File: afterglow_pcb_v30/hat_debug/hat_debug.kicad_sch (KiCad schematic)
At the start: 95 parts, among them J1 Conn_01x04_Socket, J4 Conn_01x10_Pin, J5 Conn_01x10_Pin, J7 Conn_02x03_Odd_Even, J8 Conn_02x03_Odd_Even

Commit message: Removed wrong pin headers from production files
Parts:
- J7, J8: JLCPCB C92272 -> (none)
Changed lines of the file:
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@@
 			)
 		)
-		(property "JLCPCB" "C92272"
+		(property "JLCPCB" ""
 			(at 52.705 164.465 0)
 			(effects
@@
 			)
 		)
-		(property "JLCPCB" "C92272"
+		(property "JLCPCB" ""
 			(at 47.625 113.665 0)
 			(effects

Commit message: Fixed debug hat
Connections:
- net D_SCL: now also J8.3 (Pin_3); no longer J8.4 (Pin_4)
- net D_SDA: now also J8.6 (Pin_6); no longer J8.5 (Pin_5)
- net GND: now also J8.5 (Pin_5); no longer J8.6 (Pin_6)
- net OUT_CLK: now also J8.2 (Pin_2); no longer J8.1 (Pin_1)
- net OUT_DATA: now also J8.1 (Pin_1); no longer J8.2 (Pin_2)
- net OUT_LOAD: now also J8.4 (Pin_4); no longer J8.3 (Pin_3)
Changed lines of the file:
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@@
 	(symbol
 		(lib_id "Connector_Generic:Conn_02x03_Odd_Even")
-		(at 52.705 164.465 0)
+		(at 55.245 164.465 0)
+		(mirror y)
 		(unit 1)
 		(exclude_from_sim no)
@@
 		)
 		(property "Footprint" "Connector_PinHeader_2.54mm:PinHeader_2x03_P2.54mm_Vertical"
-			(at 52.705 164.465 0)
+			(at 55.245 164.465 0)
 			(effects
 				(font
@@
 		)
 		(property "Datasheet" "~"
-			(at 52.705 164.465 0)
+			(at 55.245 164.465 0)
 			(effects
 				(font
@@
 		)
 		(property "Description" ""
-			(at 52.705 164.465 0)
+			(at 55.245 164.465 0)
 			(effects
 				(font
@@
 		)
 		(property "JLCPCB" ""
-			(at 52.705 164.465 0)
+			(at 55.245 164.465 0)
 			(effects
 				(font

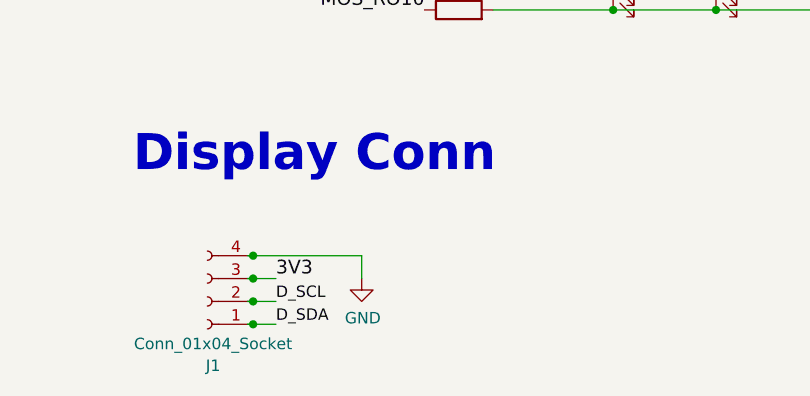
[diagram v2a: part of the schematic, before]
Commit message: Added i2c pullup resistors
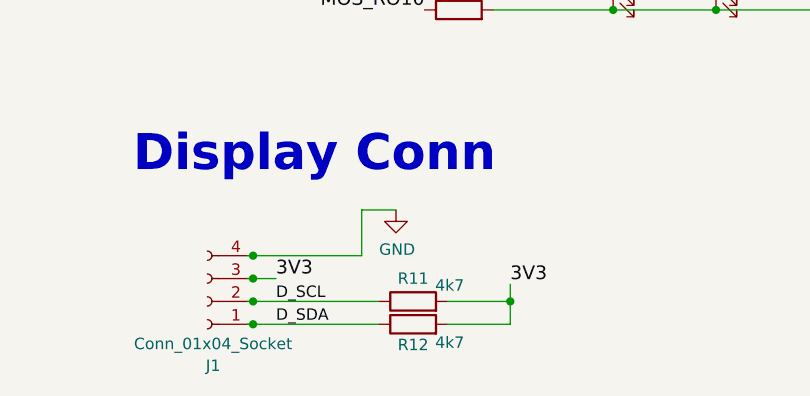
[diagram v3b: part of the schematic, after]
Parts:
- added R11, R12: 4k7, Resistor_SMD:R_0805_2012Metric, symbol Device:R
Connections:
- net 3V3: now also R11.2, R12.2
- net D_SCL: now also R11.1
- net D_SDA: now also R12.1
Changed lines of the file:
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@@
 	)
 	(junction
+		(at 149.225 177.8)
+		(diameter 0)
+		(color 0 0 0 0)
+	)
+	(junction
 		(at 206.375 122.555)
 		(diameter 0)
@@
 	(wire
 		(pts
+			(xy 149.225 175.895) (xy 149.225 177.8)
+		)
+		(stroke
+			(width 0)
+			(type default)
+		)
+	)
+	(wire
+		(pts
 			(xy 38.1 48.895) (xy 34.925 48.895)
 		)
@@
 	(wire
 		(pts
+			(xy 149.225 180.34) (xy 142.24 180.34)
+		)
+		(stroke
+			(width 0)
+			(type default)
+		)
+	)
+	(wire
+		(pts
 			(xy 194.945 88.265) (xy 183.515 88.265)
 		)
@@
 	(wire
 		(pts
+			(xy 149.225 177.8) (xy 149.225 180.34)
+		)
+		(stroke
+			(width 0)
+			(type default)
+		)
+	)
+	(wire
+		(pts
 			(xy 172.085 57.785) (xy 168.275 57.785)
 		)
@@
 	(wire
 		(pts
-			(xy 120.65 180.34) (xy 123.19 180.34)
+			(xy 120.65 180.34) (xy 134.62 180.34)
 		)
 		(stroke
@@
 	(wire
 		(pts
-			(xy 120.65 177.8) (xy 123.19 177.8)
+			(xy 120.65 177.8) (xy 134.62 177.8)
 		)
 		(stroke
@@
 	(wire
 		(pts
-			(xy 132.715 172.72) (xy 132.715 175.26)
-		)
-		(stroke
-			(width 0)
-			(type default)
-		)
-	)
-	(wire
-		(pts
 			(xy 236.855 80.645) (xy 236.855 92.075)
 		)
@@
 	(wire
 		(pts
+			(xy 132.715 172.72) (xy 132.715 167.64)
+		)
+		(stroke
+			(width 0)
+			(type default)
+		)
+	)
+	(wire
+		(pts
 			(xy 225.425 69.215) (xy 229.235 69.215)
 		)
@@
 	(wire
 		(pts
+			(xy 132.715 167.64) (xy 136.525 167.64)
+		)
+		(stroke
+			(width 0)
+			(type default)
+		)
+	)
+	(wire
+		(pts
 			(xy 146.05 65.405) (xy 160.655 65.405)
 		)
@@
 	(wire
 		(pts
+			(xy 142.24 177.8) (xy 149.225 177.8)
+		)
+		(stroke
+			(width 0)
+			(type default)
+		)
+	)
+	(wire
+		(pts
 			(xy 202.565 46.355) (xy 202.565 57.785)
 		)
@@
 		)
 	)
+	(label "3V3"
+		(at 149.225 175.895 0)
+		(fields_autoplaced yes)
+		(effects
+			(font
+				(size 1.524 1.524)
+			)
+			(justify left bottom)
+		)
+	)
 	(label "MOS_CO8"
 		(at 236.855 29.845 180)
@@
 	(symbol
 		(lib_id "power:GND")
-		(at 132.715 175.26 0)
+		(at 136.525 167.64 0)
 		(unit 1)
 		(exclude_from_sim no)
@@
 		(dnp no)
 		(property "Reference" "#PWR01"
-			(at 132.715 181.61 0)
+			(at 136.525 173.99 0)
 			(effects
 				(font
@@
 		)
 		(property "Value" "GND"
-			(at 132.842 179.6542 0)
+			(at 136.652 172.0342 0)
 			(effects
 				(font
@@
 		)
 		(property "Footprint" ""
-			(at 132.715 175.26 0)
+			(at 136.525 167.64 0)
 			(effects
 				(font
@@
 		)
 		(property "Datasheet" ""
-			(at 132.715 175.26 0)
+			(at 136.525 167.64 0)
 			(effects
 				(font
@@
 		)
 		(property "Description" ""
-			(at 132.715 175.26 0)
+			(at 136.525 167.64 0)
 			(effects
 				(font
@@
 	)
 	(symbol
+		(lib_id "Device:R")
+		(at 138.43 177.8 90)
+		(unit 1)
+		(exclude_from_sim no)
+		(in_bom yes)
+		(on_board yes)
+		(dnp no)
+		(property "Reference" "R11"
+			(at 138.43 175.26 90)
+			(effects
+				(font
+					(size 1.27 1.27)
+				)
+			)
+		)
+		(property "Value" "4k7"
+			(at 142.494 176.022 90)
+			(effects
+				(font
+					(size 1.27 1.27)
+				)
+			)
+		)
+		(property "Footprint" "Resistor_SMD:R_0805_2012Metric"
+			(at 138.43 179.578 90)
+			(effects
+				(font
+					(size 1.27 1.27)
+				)
+				(hide yes)
+			)
+		)
+		(property "Datasheet" "~"
+			(at 138.43 177.8 0)
+			(effects
+				(font
+					(size 1.27 1.27)
+				)
+				(hide yes)
+			)
+		)
+		(property "Description" "Resistor"
+			(at 138.43 177.8 0)
+			(effects
+				(font
+					(size 1.27 1.27)
+				)
+				(hide yes)
+			)
+		)
+		(property "JLCPCB" "C17673"
+			(at 138.43 177.8 90)
+			(effects
+				(font
+					(size 1.524 1.524)
+				)
+				(hide yes)
+			)
+		)
+		(pin "2"
+		)
+		(pin "1"
+		)
+		(instances
+			(project "hat_debug"
+				(path "/86dc7a78-7d51-4111-9eea-8a8f7977eb16"
+					(reference "R11")
+					(unit 1)
+				)
+			)
+		)
+	)
+	(symbol
 		(lib_id "Connector_Generic:Conn_02x03_Odd_Even")
 		(at 55.245 164.465 0)
@@
 					(unit 1)
 				)
+			)
+		)
+	)
+	(symbol
+		(lib_id "Device:R")
+		(at 138.43 180.34 90)
+		(unit 1)
+		(exclude_from_sim no)
+		(in_bom yes)
+		(on_board yes)
+		(dnp no)
+		(property "Reference" "R12"
+			(at 138.43 182.626 90)
+			(effects
+				(font
+					(size 1.27 1.27)
+				)
+			)
+		)
+		(property "Value" "4k7"
+			(at 142.494 182.372 90)
+			(effects
+				(font
+					(size 1.27 1.27)
+				)
+			)
+		)
+		(property "Footprint" "Resistor_SMD:R_0805_2012Metric"
+			(at 138.43 182.118 90)
+			(effects
+				(font
+					(size 1.27 1.27)
+				)
+				(hide yes)
+			)
+		)
+		(property "Datasheet" "~"
+			(at 138.43 180.34 0)
+			(effects
+				(font
+					(size 1.27 1.27)
+				)
+				(hide yes)
+			)
+		)
+		(property "Description" "Resistor"
+			(at 138.43 180.34 0)
+			(effects
+				(font
+					(size 1.27 1.27)
+				)
+				(hide yes)
+			)
+		)
+		(property "JLCPCB" "C17673"
+			(at 138.43 180.34 90)
+			(effects
+				(font
+					(size 1.524 1.524)
+				)
+				(hide yes)
+			)
+		)
+		(pin "2"
+		)
+		(pin "1"
+		)
+		(instances
+			(project "hat_debug"
+				(path "/86dc7a78-7d51-4111-9eea-8a8f7977eb16"
+					(reference "R12")
+					(unit 1)
+				)
